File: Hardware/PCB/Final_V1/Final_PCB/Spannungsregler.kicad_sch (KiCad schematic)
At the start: 6 parts, among them U1 TPS63000-Q1

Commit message: fixing xhematics
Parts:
- renumbered R1 to R13, R2 to R14
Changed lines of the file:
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@@
 		(dnp no)
 		(fields_autoplaced yes)
-		(property "Reference" "R1"
+		(property "Reference" "R13"
 			(at 146.05 77.4699 0)
 			(effects
@@
 			(project "Spannungsregler"
 				(path "/3cedac76-cdf6-4427-9720-a412bd9af7e2/d799d98f-baa1-4663-b197-1e0a5357dff3"
-					(reference "R1")
+					(reference "R13")
 					(unit 1)
 				)
@@
 		(dnp no)
 		(fields_autoplaced yes)
-		(property "Reference" "#PWR04"
+		(property "Reference" "#PWR0112"
 			(at 107.95 109.22 0)
 			(effects
@@
 			(project "Spannungsregler"
 				(path "/3cedac76-cdf6-4427-9720-a412bd9af7e2/d799d98f-baa1-4663-b197-1e0a5357dff3"
-					(reference "#PWR04")
+					(reference "#PWR0112")
 					(unit 1)
 				)
@@
 		(dnp no)
 		(fields_autoplaced yes)
-		(property "Reference" "R2"
+		(property "Reference" "R14"
 			(at 146.05 87.6299 0)
 			(effects
@@
 			(project "Spannungsregler"
 				(path "/3cedac76-cdf6-4427-9720-a412bd9af7e2/d799d98f-baa1-4663-b197-1e0a5357dff3"
-					(reference "R2")
+					(reference "R14")
 					(unit 1)
 				)
@@
 		(dnp no)
 		(fields_autoplaced yes)
-		(property "Reference" "#PWR02"
+		(property "Reference" "#PWR0113"
 			(at 127 109.22 0)
 			(effects
@@
 			(project "Spannungsregler"
 				(path "/3cedac76-cdf6-4427-9720-a412bd9af7e2/d799d98f-baa1-4663-b197-1e0a5357dff3"
-					(reference "#PWR02")
+					(reference "#PWR0113")
 					(unit 1)
 				)
@@
 		(dnp no)
 		(fields_autoplaced yes)
-		(property "Reference" "#PWR05"
+		(property "Reference" "#PWR0111"
 			(at 154.94 109.22 0)
 			(effects
@@
 			(project "Spannungsregler"
 				(path "/3cedac76-cdf6-4427-9720-a412bd9af7e2/d799d98f-baa1-4663-b197-1e0a5357dff3"
-					(reference "#PWR05")
+					(reference "#PWR0111")
 					(unit 1)
 				)
@@
 		(dnp no)
 		(fields_autoplaced yes)
-		(property "Reference" "#PWR03"
+		(property "Reference" "#PWR0115"
 			(at 154.94 76.2 0)
 			(effects
@@
 			(project "Spannungsregler"
 				(path "/3cedac76-cdf6-4427-9720-a412bd9af7e2/d799d98f-baa1-4663-b197-1e0a5357dff3"
-					(reference "#PWR03")
+					(reference "#PWR0115")
 					(unit 1)
 				)
@@
 		(dnp no)
 		(fields_autoplaced yes)
-		(property "Reference" "#PWR01"
+		(property "Reference" "#PWR0114"
 			(at 143.51 109.22 0)
 			(effects
@@
 			(project "Spannungsregler"
 				(path "/3cedac76-cdf6-4427-9720-a412bd9af7e2/d799d98f-baa1-4663-b197-1e0a5357dff3"
-					(reference "#PWR01")
-					(unit 1)
-				)
+					(reference "#PWR0114")
+					(unit 1)
+				)

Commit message: reapplied fixes because of commiting problems
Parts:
- added C11: 0.1uF, symbol Device:C
- added R3: 100, Resistor_SMD:R_0603_1608Metric, symbol Device:R
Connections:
- net Bat_Voltage: now also R3.1; no longer U1.6 (EN), U1.7 (PS/SYNC), U1.8 (VINA)
- net GND: now also C11.2
- new net: C11.1, R3.2
- new net: U1.6 (EN), U1.7 (PS/SYNC), U1.8 (VINA)
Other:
- moved on the sheet: C1

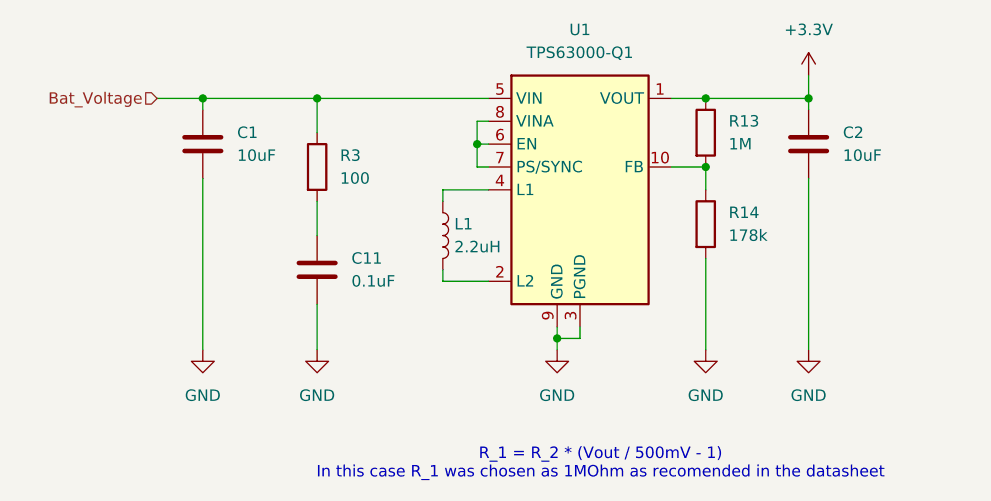
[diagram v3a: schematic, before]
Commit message: fixed some minor mistakes and added test pads for the battery charger
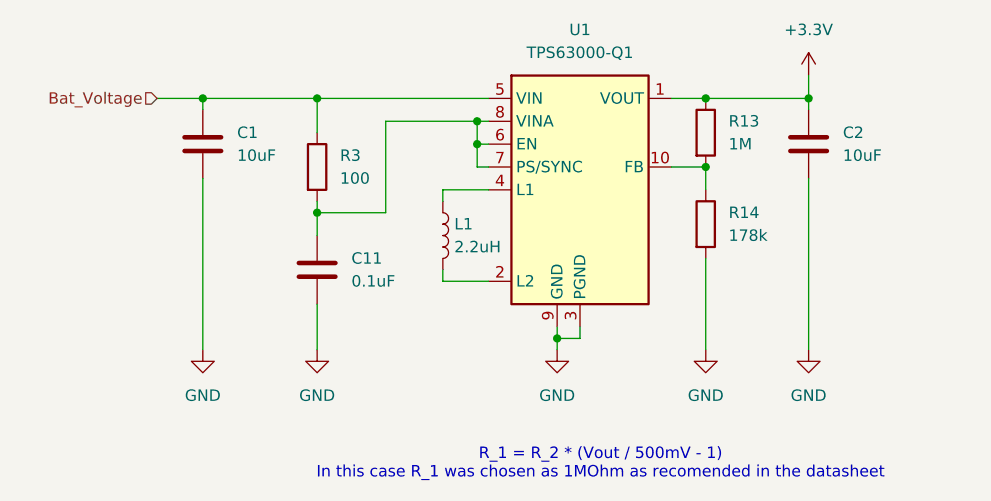
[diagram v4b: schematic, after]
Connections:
- net at C11.1, R3.2: now also U1.6 (EN), U1.7 (PS/SYNC), U1.8 (VINA)
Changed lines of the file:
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@@
+	)
+	(junction
+		(at 100.33 87.63)
+		(diameter 0)
+		(color 0 0 0 0)
+	)
+	(junction
+		(at 118.11 77.47)
+		(diameter 0)
+		(color 0 0 0 0)
 	)
 	(junction
@@
 	(wire
 		(pts
+			(xy 100.33 87.63) (xy 100.33 90.17)
+		)
+		(stroke
+			(width 0)
+			(type default)
+		)
+	)
+	(wire
+		(pts
 			(xy 127 101.6) (xy 127 102.87)
 		)
@@
 	(wire
 		(pts
+			(xy 107.95 77.47) (xy 107.95 87.63)
+		)
+		(stroke
+			(width 0)
+			(type default)
+		)
+	)
+	(wire
+		(pts
+			(xy 118.11 77.47) (xy 107.95 77.47)
+		)
+		(stroke
+			(width 0)
+			(type default)
+		)
+	)
+	(wire
+		(pts
 			(xy 82.55 74.93) (xy 87.63 74.93)
 		)
@@
 	(wire
 		(pts
-			(xy 100.33 86.36) (xy 100.33 90.17)
-		)
-		(stroke
+			(xy 107.95 87.63) (xy 100.33 87.63)
+		)
+		(stroke
+			(width 0)
+			(type default)
+		)
+	)
+	(wire
+		(pts
+			(xy 100.33 86.36) (xy 100.33 87.63)
+		)
+		(stroke

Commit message: #4: Layout-Session-17-11-25
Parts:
- C11, C2: footprint (none) -> Capacitor_SMD:C_0603_1608Metric
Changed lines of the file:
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@@
 			)
 		)
-		(property "Footprint" ""
+		(property "Footprint" "Capacitor_SMD:C_0603_1608Metric"
 			(at 155.9052 83.82 0)
 			(effects
@@
 			)
 		)
-		(property "Footprint" ""
+		(property "Footprint" "Capacitor_SMD:C_0603_1608Metric"
 			(at 101.2952 97.79 0)
 			(effects
